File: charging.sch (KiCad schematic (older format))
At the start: 8 parts, among them U2 TP4056

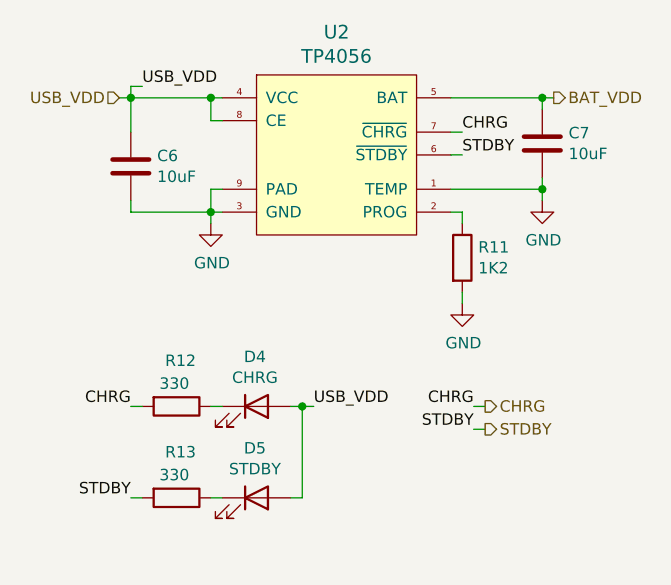
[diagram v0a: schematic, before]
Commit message: Запитал МК, добавил цепи питания, тактирования, модуль клавиатуры.
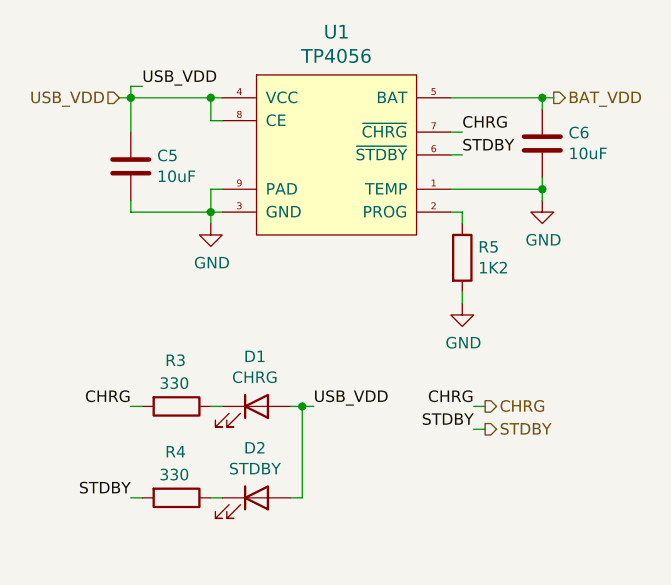
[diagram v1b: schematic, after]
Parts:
- renumbered C6 to C5, C7 to C6, D4 to D1, D5 to D2, R12 to R3, R13 to R4, R11 to R5, U2 to U1
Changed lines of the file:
@@
 $Descr A4 11693 8268
 encoding utf-8
-Sheet 5 5
+Sheet 4 9
 Title ""
 Date ""
@@
 Connection ~ 5350 3000
 $Comp
-L Device:C C6
+L Device:C C5
 U 1 1 5EA9A9B6
 P 5000 3300
-F 0 "C6" H 5115 3346 50  0000 L CNN
+F 0 "C5" H 5115 3346 50  0000 L CNN
 F 1 "10uF" H 5115 3255 50  0000 L CNN
 F 2 "Capacitor_SMD:C_0805_2012Metric_Pad1.15x1.40mm_HandSolder" H 5038 3150 50  0001 C CNN
@@
 BAT_VDD
 $Comp
-L power:GND #PWR019
+L power:GND #PWR010
 U 1 1 5EA9CBD2
 P 6450 3900
-F 0 "#PWR019" H 6450 3650 50  0001 C CNN
+F 0 "#PWR010" H 6450 3650 50  0001 C CNN
 F 1 "GND" H 6455 3727 50  0000 C CNN
 F 2 "" H 6450 3900 50  0001 C CNN
@@
 $EndComp
 $Comp
-L Device:R R11
+L Device:R R5
 U 1 1 5EA9D067
 P 6450 3700
-F 0 "R11" H 6520 3746 50  0000 L CNN
+F 0 "R5" H 6520 3746 50  0000 L CNN
 F 1 "1K2" H 6520 3655 50  0000 L CNN
 F 2 "Resistor_SMD:R_0603_1608Metric_Pad1.05x0.95mm_HandSolder" V 6380 3700 50  0001 C CNN
@@
 $EndComp
 $Comp
-L power:GND #PWR020
+L power:GND #PWR011
 U 1 1 5EA9ED22
 P 6800 3450
-F 0 "#PWR020" H 6800 3200 50  0001 C CNN
+F 0 "#PWR011" H 6800 3200 50  0001 C CNN
 F 1 "GND" H 6805 3277 50  0000 C CNN
 F 2 "" H 6800 3450 50  0001 C CNN
@@
 	6800 3400 6800 3450
 $Comp
-L Device:C C7
+L Device:C C6
 U 1 1 5EAA122E
 P 6800 3200
-F 0 "C7" H 6915 3246 50  0000 L CNN
+F 0 "C6" H 6915 3246 50  0000 L CNN
 F 1 "10uF" H 6915 3155 50  0000 L CNN
 F 2 "Capacitor_SMD:C_0805_2012Metric_Pad1.15x1.40mm_HandSolder" H 6838 3050 50  0001 C CNN
@@
 	6450 3850 6450 3900
 $Comp
-L Device:LED D4
+L Device:LED D1
 U 1 1 5EAB145B
 P 5550 4350
-F 0 "D4" H 5543 4567 50  0000 C CNN
+F 0 "D1" H 5543 4567 50  0000 C CNN
 F 1 "CHRG" H 5543 4476 50  0000 C CNN
 F 2 "LED_SMD:LED_0603_1608Metric_Pad1.05x0.95mm_HandSolder" H 5550 4350 50  0001 C CNN
@@
 $EndComp
 $Comp
-L Device:LED D5
+L Device:LED D2
 U 1 1 5EAB1A26
 P 5550 4750
-F 0 "D5" H 5543 4967 50  0000 C CNN
+F 0 "D2" H 5543 4967 50  0000 C CNN
 F 1 "STDBY" H 5543 4876 50  0000 C CNN
 F 2 "LED_SMD:LED_0603_1608Metric_Pad1.05x0.95mm_HandSolder" H 5550 4750 50  0001 C CNN
@@
 $EndComp
 $Comp
-L Device:R R12
+L Device:R R3
 U 1 1 5EAB1D19
 P 5200 4350
-F 0 "R12" V 5000 4300 50  0000 L CNN
+F 0 "R3" V 5000 4300 50  0000 L CNN
 F 1 "330" V 5100 4275 50  0000 L CNN
 F 2 "Resistor_SMD:R_0603_1608Metric_Pad1.05x0.95mm_HandSolder" V 5130 4350 50  0001 C CNN
@@
 $EndComp
 $Comp
-L Device:R R13
+L Device:R R4
 U 1 1 5EAB3B1E
 P 5200 4750
-F 0 "R13" V 5000 4700 50  0000 L CNN
+F 0 "R4" V 5000 4700 50  0000 L CNN
 F 1 "330" V 5100 4675 50  0000 L CNN
 F 2 "Resistor_SMD:R_0603_1608Metric_Pad1.05x0.95mm_HandSolder" V 5130 4750 50  0001 C CNN
@@
 	6500 4450 6550 4450
 $Comp
-L tp4056:TP4056 U2
+L tp4056:TP4056 U1
 U 1 1 5EAE2027
 P 5900 3250
-F 0 "U2" H 5900 3787 60  0000 C CNN
+F 0 "U1" H 5900 3787 60  0000 C CNN
 F 1 "TP4056" H 5900 3681 60  0000 C CNN
 F 2 "Package_SO:HSOP-8-1EP_3.9x4.9mm_P1.27mm_EP2.41x3.1mm_ThermalVias" H 5900 3250 60  0001 C CNN

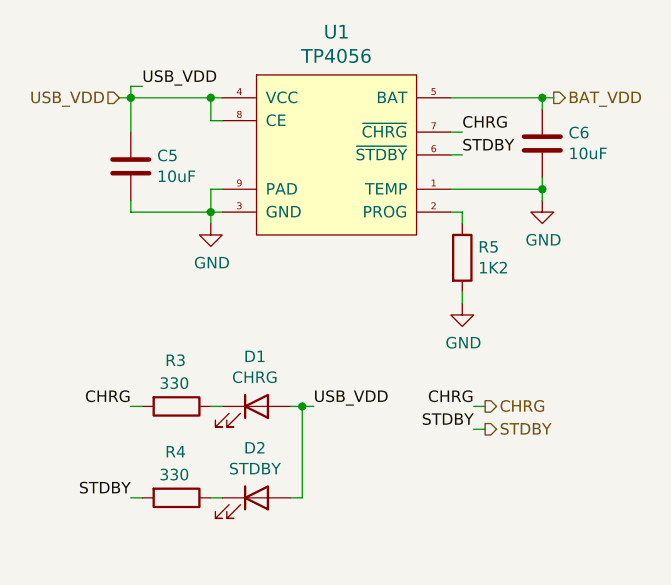
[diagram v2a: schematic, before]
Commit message: dcdc доделан на 5V.
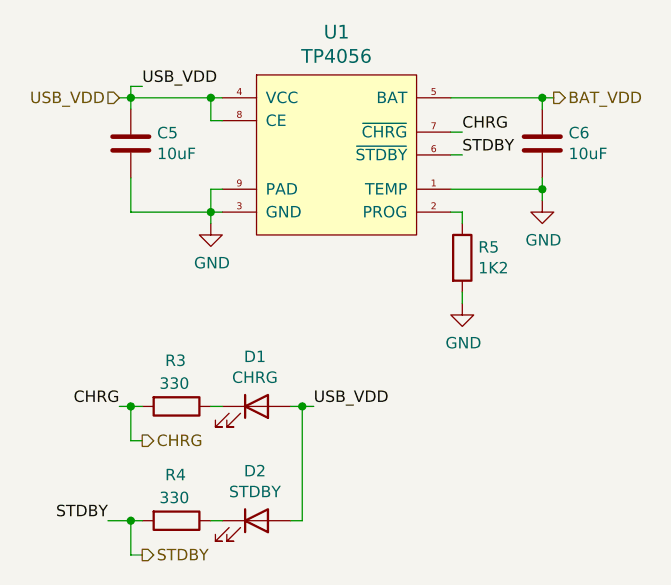
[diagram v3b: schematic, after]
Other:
- moved on the sheet: C5, D2, R4
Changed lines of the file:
@@
 L Device:C C5
 U 1 1 5EA9A9B6
-P 5000 3300
-F 0 "C5" H 5115 3346 50  0000 L CNN
-F 1 "10uF" H 5115 3255 50  0000 L CNN
-F 2 "Capacitor_SMD:C_0805_2012Metric_Pad1.15x1.40mm_HandSolder" H 5038 3150 50  0001 C CNN
-F 3 "~" H 5000 3300 50  0001 C CNN
-	1    5000 3300
+P 5000 3200
+F 0 "C5" H 5115 3246 50  0000 L CNN
+F 1 "10uF" H 5115 3155 50  0000 L CNN
+F 2 "Capacitor_SMD:C_0805_2012Metric_Pad1.15x1.40mm_HandSolder" H 5038 3050 50  0001 C CNN
+F 3 "~" H 5000 3200 50  0001 C CNN
+	1    5000 3200
 	1    0    0    -1
 $EndComp
 Wire Wire Line
-	5000 3150 5000 3000
+	5000 3050 5000 3000
 Wire Wire Line
 	5000 3000 4950 3000
 Wire Wire Line
-	5000 3450 5000 3500
+	5000 3350 5000 3500
 Wire Wire Line
 	5000 3500 5350 3500
@@
 L Device:LED D2
 U 1 1 5EAB1A26
-P 5550 4750
-F 0 "D2" H 5543 4967 50  0000 C CNN
-F 1 "STDBY" H 5543 4876 50  0000 C CNN
-F 2 "LED_SMD:LED_0603_1608Metric_Pad1.05x0.95mm_HandSolder" H 5550 4750 50  0001 C CNN
-F 3 "~" H 5550 4750 50  0001 C CNN
-	1    5550 4750
+P 5550 4850
+F 0 "D2" H 5543 5067 50  0000 C CNN
+F 1 "STDBY" H 5543 4976 50  0000 C CNN
+F 2 "LED_SMD:LED_0603_1608Metric_Pad1.05x0.95mm_HandSolder" H 5550 4850 50  0001 C CNN
+F 3 "~" H 5550 4850 50  0001 C CNN
+	1    5550 4850
 	1    0    0    -1
 $EndComp
@@
 L Device:R R4
 U 1 1 5EAB3B1E
-P 5200 4750
-F 0 "R4" V 5000 4700 50  0000 L CNN
-F 1 "330" V 5100 4675 50  0000 L CNN
-F 2 "Resistor_SMD:R_0603_1608Metric_Pad1.05x0.95mm_HandSolder" V 5130 4750 50  0001 C CNN
-F 3 "~" H 5200 4750 50  0001 C CNN
-	1    5200 4750
+P 5200 4850
+F 0 "R4" V 5000 4800 50  0000 L CNN
+F 1 "330" V 5100 4775 50  0000 L CNN
+F 2 "Resistor_SMD:R_0603_1608Metric_Pad1.05x0.95mm_HandSolder" V 5130 4850 50  0001 C CNN
+F 3 "~" H 5200 4850 50  0001 C CNN
+	1    5200 4850
 	0    1    1    0
 $EndComp
-Text Label 5000 4350 2    50   ~ 0
+Text Label 4950 4350 2    50   ~ 0
 CHRG
-Text Label 5000 4750 2    50   ~ 0
+Text Label 4900 4850 2    50   ~ 0
 STDBY
-Wire Wire Line
-	5000 4350 5050 4350
-Wire Wire Line
-	5000 4750 5050 4750
 Wire Wire Line
 	5350 4350 5400 4350
 Wire Wire Line
-	5350 4750 5400 4750
+	5350 4850 5400 4850
 Text Label 5050 2950 0    50   ~ 0
 USB_VDD
@@
 USB_VDD
 Wire Wire Line
-	5700 4750 5750 4750
-Wire Wire Line
-	5750 4750 5750 4350
-Wire Wire Line
-	5750 4350 5800 4350
-Wire Wire Line
-	5750 4350 5700 4350
-Connection ~ 5750 4350
-Text HLabel 6550 4350 2    50   Output ~ 0
+	5700 4850 5750 4850
+Text HLabel 5050 4500 2    50   Output ~ 0
 CHRG
-Text Label 6500 4350 2    50   ~ 0
-CHRG
-Wire Wire Line
-	6500 4350 6550 4350
-Text HLabel 6550 4450 2    50   Output ~ 0
+Text HLabel 5050 5000 2    50   Output ~ 0
 STDBY
-Text Label 6500 4450 2    50   ~ 0
-STDBY
-Wire Wire Line
-	6500 4450 6550 4450
 $Comp
 L tp4056:TP4056 U1
@@
 	1    0    0    -1
 $EndComp
+Wire Wire Line
+	5700 4350 5750 4350
+Wire Wire Line
+	4950 4350 5000 4350
+Wire Wire Line
+	5000 4350 5000 4500
+Wire Wire Line
+	5000 4500 5050 4500
+Connection ~ 5000 4350
+Wire Wire Line
+	5000 4350 5050 4350
+Wire Wire Line
+	4900 4850 5000 4850
+Wire Wire Line
+	5000 4850 5000 5000
+Wire Wire Line
+	5000 5000 5050 5000
+Connection ~ 5000 4850
+Wire Wire Line
+	5000 4850 5050 4850
+Wire Wire Line
+	5750 4350 5750 4850
+Connection ~ 5750 4350
+Wire Wire Line
+	5750 4350 5800 4350
 $EndSCHEMATC

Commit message: Расставил проверенные блоки в столбец.
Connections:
- net BAT_VDD renamed VDD_BAT
- net USB_VDD renamed VDD_USB
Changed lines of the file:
@@
 	5350 3100 5400 3100
 Text HLabel 4950 3000 0    50   Input ~ 0
-USB_VDD
+VDD_USB
 Connection ~ 5350 3000
 $Comp
@@
 Connection ~ 5000 3000
 Text HLabel 6850 3000 2    50   Output ~ 0
-BAT_VDD
+VDD_BAT
 $Comp
 L power:GND #PWR010
@@
 	5350 4850 5400 4850
 Text Label 5050 2950 0    50   ~ 0
-USB_VDD
+VDD_USB
 Wire Wire Line
 	5000 3000 5000 2950
@@
 	5000 2950 5050 2950
 Text Label 5800 4350 0    50   ~ 0
-USB_VDD
+VDD_USB
 Wire Wire Line
 	5700 4850 5750 4850
